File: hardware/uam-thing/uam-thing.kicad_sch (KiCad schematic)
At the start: 2 parts, among them J1 ESP_Left, J2 ESP_Right

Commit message: First version of hardware design
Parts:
- added C1: 1.0uF, Capacitor_THT:CP_Radial_D5.0mm_P2.00mm, symbol Device:C_Polarized
- added C2, C3, C4, C5: 470pF, Capacitor_THT:C_Disc_D4.7mm_W2.5mm_P5.00mm, symbol Device:C
- added C6: 0.01uF, Capacitor_THT:C_Disc_D4.7mm_W2.5mm_P5.00mm, symbol Device:C_Polarized
- added J10: SFM_A, Connector_JST:JST_XH_B6B-XH-A_1x06_P2.50mm_Vertical, symbol Connector:Conn_01x06_Female
- added J11: SFM_C, Connector_JST:JST_XH_B6B-XH-A_1x06_P2.50mm_Vertical, symbol Connector:Conn_01x06_Female
- added J12: SFM_D, Connector_JST:JST_XH_B6B-XH-A_1x06_P2.50mm_Vertical, symbol Connector:Conn_01x06_Female
- added J3: PCA_Left, symbol Connector:Conn_01x12_Female
- added J4: PCA_Right, symbol Connector:Conn_01x12_Female
- added J5: MPX_A, symbol Connector:Conn_01x06_Female
- added J6: MPX_B, symbol Connector:Conn_01x06_Female
- added J7: MPX_C, Connector_PinHeader_2.54mm:PinHeader_1x06_P2.54mm_Vertical, symbol Connector:Conn_01x06_Female
- added J8: MPX_D, Connector_PinHeader_2.54mm:PinHeader_1x06_P2.54mm_Vertical, symbol Connector:Conn_01x06_Female
- added J9: SFM_B, Connector_JST:JST_XH_B6B-XH-A_1x06_P2.50mm_Vertical, symbol Connector:Conn_01x06_Female
- added R1, R10, R11, R2, R3, R4, R5, R6, R7, R8, R9: 10k, Resistor_THT:R_Axial_DIN0207_L6.3mm_D2.5mm_P10.16mm_Horizontal, symbol Device:R_Small
- J1, J2: footprint (none) -> Connector_PinHeader_2.54mm:PinHeader_1x15_P2.54mm_Vertical
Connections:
- net +3.3V: now also J3.1 (Pin_1), R1.1, R2.2, R3.1
- net ADC1_CH4: now also J1.6 (Pin_6), C4.2, J7.1 (Pin_1); no longer J1.5 (Pin_5)
- net ADC1_CH5: now also J1.7 (Pin_7), C5.2, J8.1 (Pin_1); no longer J1.6 (Pin_6)
- net ADC1_CH6: now also J1.4 (Pin_4), C2.2, J5.1 (Pin_1); no longer J1.3 (Pin_3)
- net ADC1_CH7: now also J1.5 (Pin_5), C3.2, J6.1 (Pin_1); no longer J1.4 (Pin_4)
- net GND: now also C1.2, C2.1, C3.1, C4.1, C5.1, C6.2, J10.2 (Pin_2), J11.2 (Pin_2), J12.2 (Pin_2), J3.2 (Pin_2), J3.6 (Pin_6), J3.7 (Pin_7), J3.8 (Pin_8), J5.2 (Pin_2), J6.2 (Pin_2), J7.2 (Pin_2), J8.2 (Pin_2), J9.2 (Pin_2)
- net +5V: now reaches J1.15 (Pin_15)
- net +5V: now also C1.1, C6.1, J10.1 (Pin_1), J11.1 (Pin_1), J12.1 (Pin_1), J5.3 (Pin_3), J6.3 (Pin_3), J7.3 (Pin_3), J8.3 (Pin_3), J9.1 (Pin_1), R10.1, R11.2, R4.1, R5.2, R6.1, R7.2, R8.1, R9.2
- net SCL renamed SCL_ESP
- net SCL_ESP: now also J3.4 (Pin_4), R2.1
- net SDA renamed SDA_ESP
- net SDA_ESP: now also J3.3 (Pin_3), R1.2
- new net: J3.5 (Pin_5), R3.2
- new net SFM_A_SCL: J10.4 (Pin_4), J3.10 (Pin_10), R5.1
- new net SFM_A_SDL: J10.3 (Pin_3), J3.9 (Pin_9), R4.2
- new net SFM_B_SCL: J3.12 (Pin_12), J9.4 (Pin_4), R7.1
- new net SFM_B_SDL: J3.11 (Pin_11), J9.3 (Pin_3), R6.2
- new net SFM_C_SCL: J11.4 (Pin_4), J4.11 (Pin_11), R9.1
- new net SFM_C_SDL: J11.3 (Pin_3), J4.12 (Pin_12), R8.2
- new net SFM_D_SCL: J12.4 (Pin_4), J4.9 (Pin_9), R11.1
- new net SFM_D_SDL: J12.3 (Pin_3), J4.10 (Pin_10), R10.2
- no-connect marks 0 -> 49
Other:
- note added: "ESP32"
- note added: "I2C Multiplexer"
- note added: "MPX5100 Sensors"
- note added: "SFM3300 Sensors"
- note added: "TCA9458A"

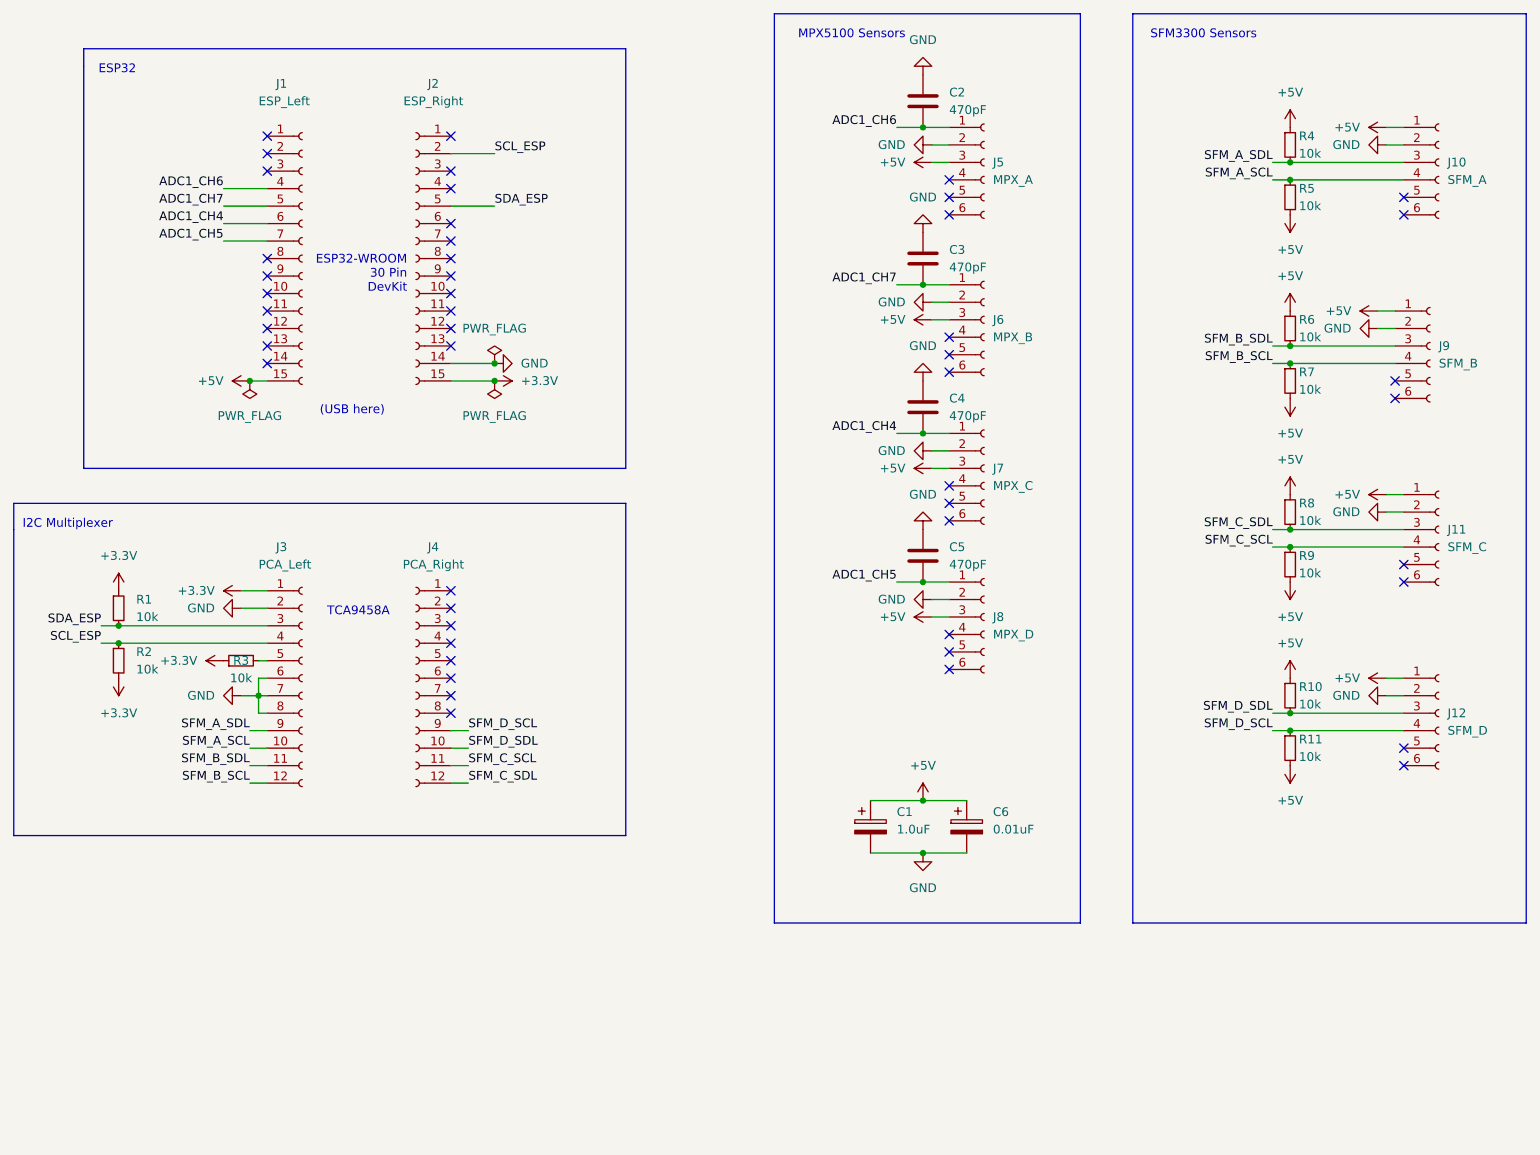
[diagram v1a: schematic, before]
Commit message: Voltage dividers for MPX sensors
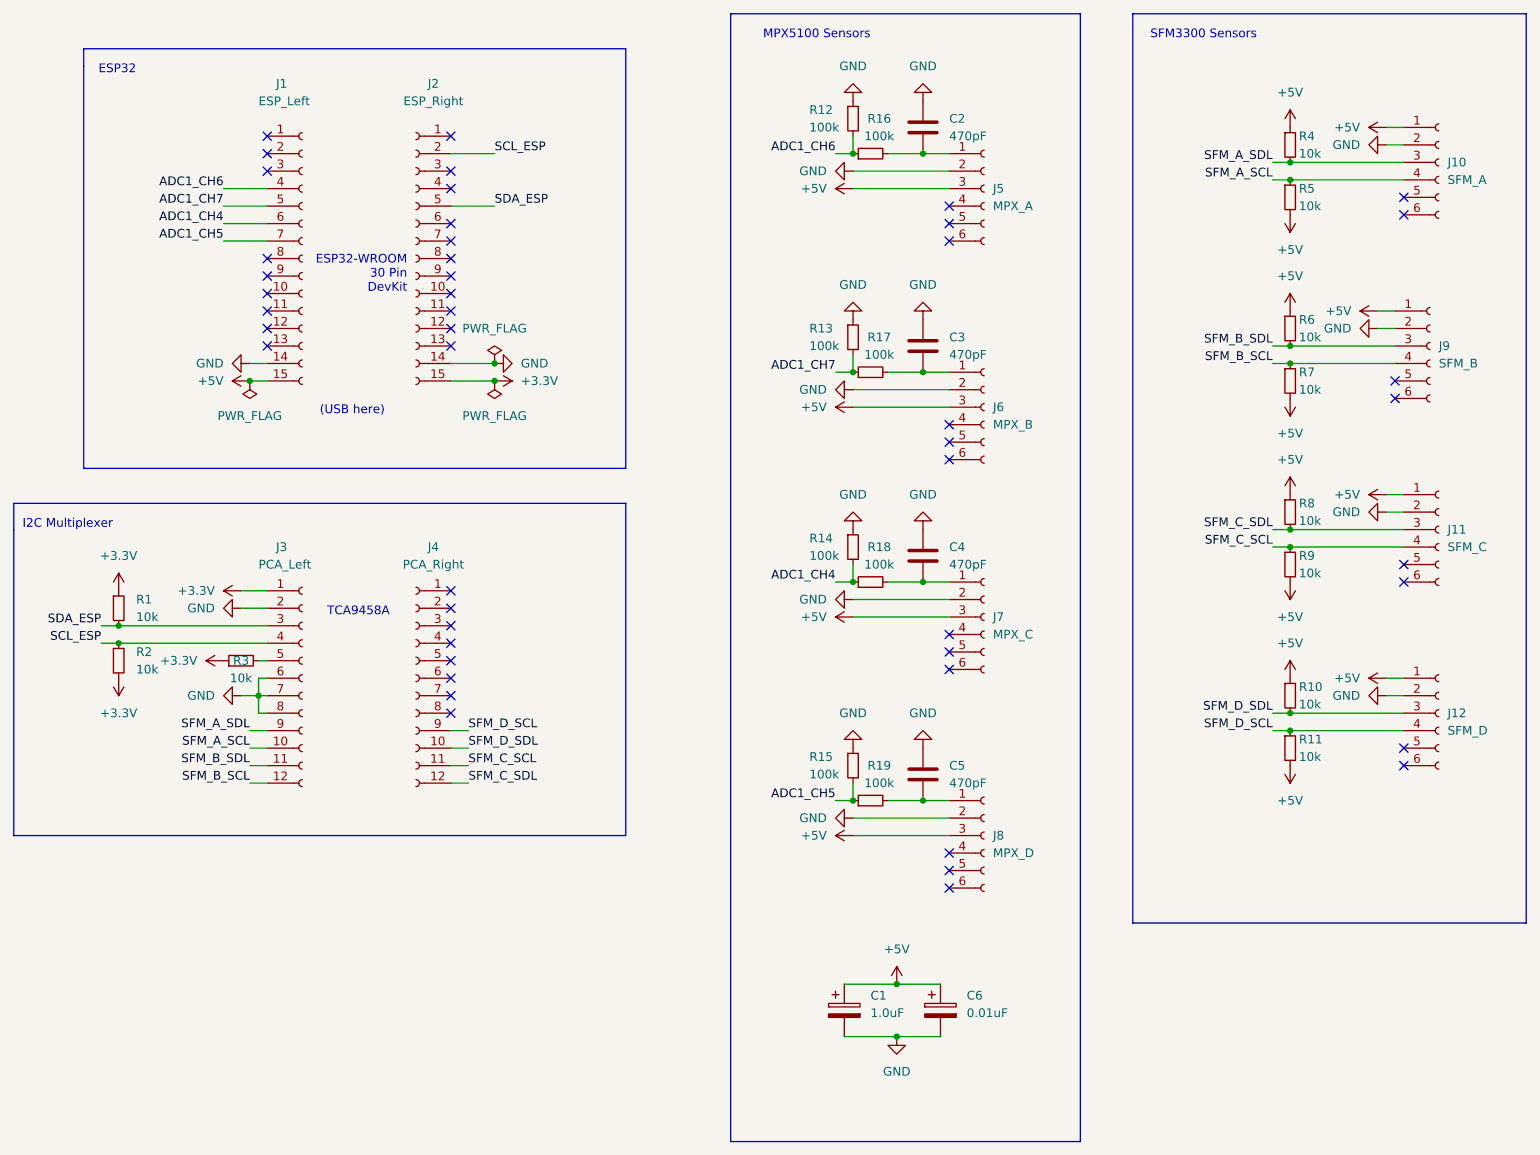
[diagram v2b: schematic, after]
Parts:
- added R12, R13, R14, R15, R16, R17, R18, R19: 100k, Resistor_THT:R_Axial_DIN0207_L6.3mm_D2.5mm_P10.16mm_Horizontal, symbol Device:R_Small
- J3, J4: footprint (none) -> Connector_PinHeader_2.54mm:PinHeader_1x12_P2.54mm_Vertical
- J5, J6: footprint (none) -> Connector_PinHeader_2.54mm:PinHeader_1x06_P2.54mm_Vertical
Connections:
- net ADC1_CH4: now also R14.2, R18.1; no longer C4.2, J7.1 (Pin_1)
- net ADC1_CH5: now also R15.2, R19.1; no longer C5.2, J8.1 (Pin_1)
- net ADC1_CH6: now also R12.2, R16.1; no longer C2.2, J5.1 (Pin_1)
- net ADC1_CH7: now also R13.2, R17.1; no longer C3.2, J6.1 (Pin_1)
- net GND: now also J1.14 (Pin_14), R12.1, R13.1, R14.1, R15.1
- new net: C4.2, J7.1 (Pin_1), R18.2
- new net: C2.2, J5.1 (Pin_1), R16.2
- new net: C3.2, J6.1 (Pin_1), R17.2
- new net: C5.2, J8.1 (Pin_1), R19.2
- no-connect marks 49 -> 48
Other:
- moved on the sheet: C1, C2, C3, C4, C5, C6, J5, J6, J7, J8

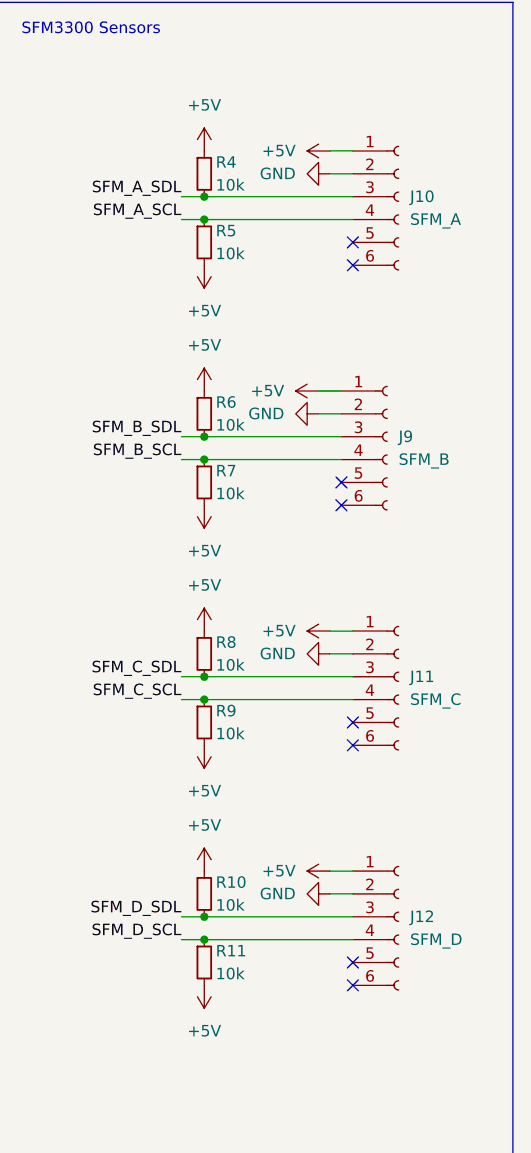
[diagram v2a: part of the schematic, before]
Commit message: Reworked PCB for 4 pin JST, replaced connectors again
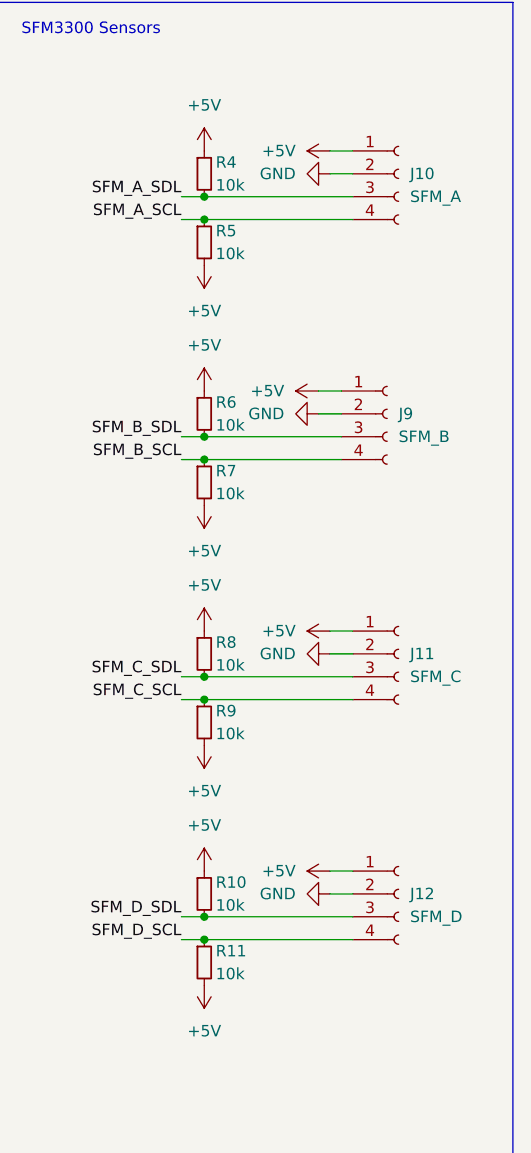
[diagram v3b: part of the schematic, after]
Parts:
- J10, J11, J12, J9: footprint Connector_JST:JST_XH_B6B-XH-A_1x06_P2.50mm_Vertical -> Connector_JST:JST_XH_B4B-XH-A_1x04_P2.50mm_Vertical; symbol Connector:Conn_01x06_Female -> Connector:Conn_01x04_Female
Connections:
- no-connect marks 48 -> 40
